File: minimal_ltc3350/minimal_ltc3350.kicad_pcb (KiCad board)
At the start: 4 copper layers, 25.4 x 25.4 mm, 0 parts

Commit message: Update KiCad project files (PCB layout, project settings, and schematic)
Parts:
- added U1: LTC3350EUHF-PBF, analog_devices_footprints:QFN-38_UHF_LIT, F.Cu at (139.7, 88.9)
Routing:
- added copper zone on B.Cu, net GND
- added copper zone on F.Cu, net GND
- added copper zone on In1.Cu, net GND
- added copper zone on In2.Cu, net GND
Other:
- outline, holes or cut-outs redrawn

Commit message: Update KiCad project files and submodule reference
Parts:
- added C1: 100 nF, capacitor_footprints:C_0402_1005Metric, F.Cu at (139.6, 83.8)
- added C2: 1 µF, capacitor_footprints:C_0603_1608Metric, F.Cu at (142.3, 83.8)
- added Q1: 20.0 V, transistor_footprints:PowerPAK 1212-8, F.Cu at (143.0, 80.9)
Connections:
- U1 pad 31: unconnected-(U1-VOUTSP-Pad31) -> /VOUTSP
- U1 pad 32: unconnected-(U1-VOUTM5-Pad32) -> /VOUTM5
- U1 pad 33: unconnected-(U1-INFET-Pad33) -> /INFET
- U1 pad 34: unconnected-(U1-VIN-Pad34) -> /VIN
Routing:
- net /INFET: track 0.00 -> 4.16 mm
- net /VOUTM5: track 0.00 -> 1.78 mm
- net /VIN: track 0.00 -> 1.71 mm

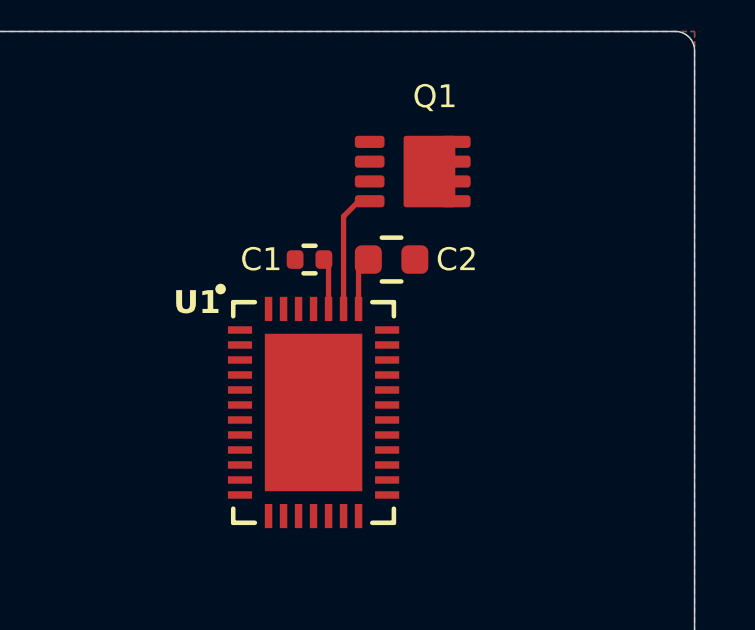
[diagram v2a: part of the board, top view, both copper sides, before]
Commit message: Add VOUT sensing resistor and update symbol libraries
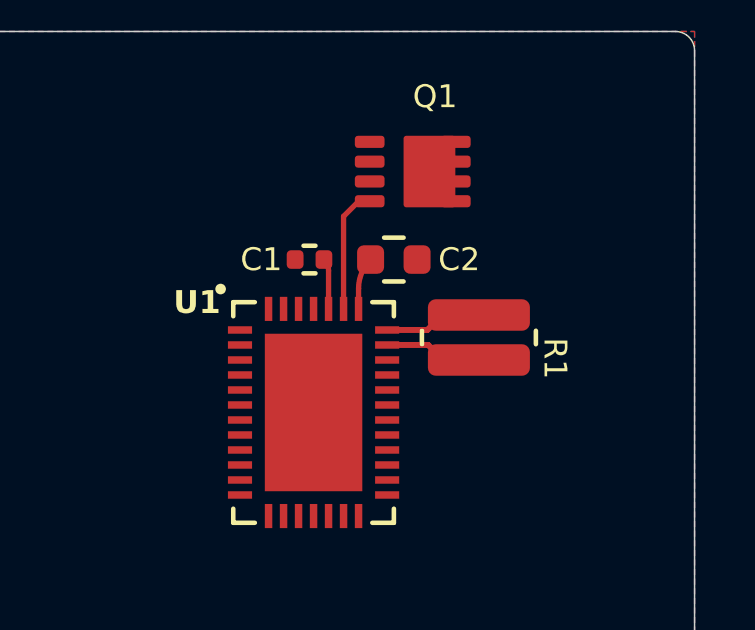
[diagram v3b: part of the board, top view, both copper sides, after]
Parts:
- added R1: 0.016 Ω, resistor_footprints:R_0612_1632Metric, F.Cu at (145.2, 86.4)
- moved C2 0.08 mm to (142.4, 83.8)
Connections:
- U1 pad 30: unconnected-(U1-VOUTSN-Pad30) -> /VOUT
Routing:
- net /VOUT: track 0.00 -> 3.27 mm
- net /VOUTSP: track 0.00 -> 3.27 mm

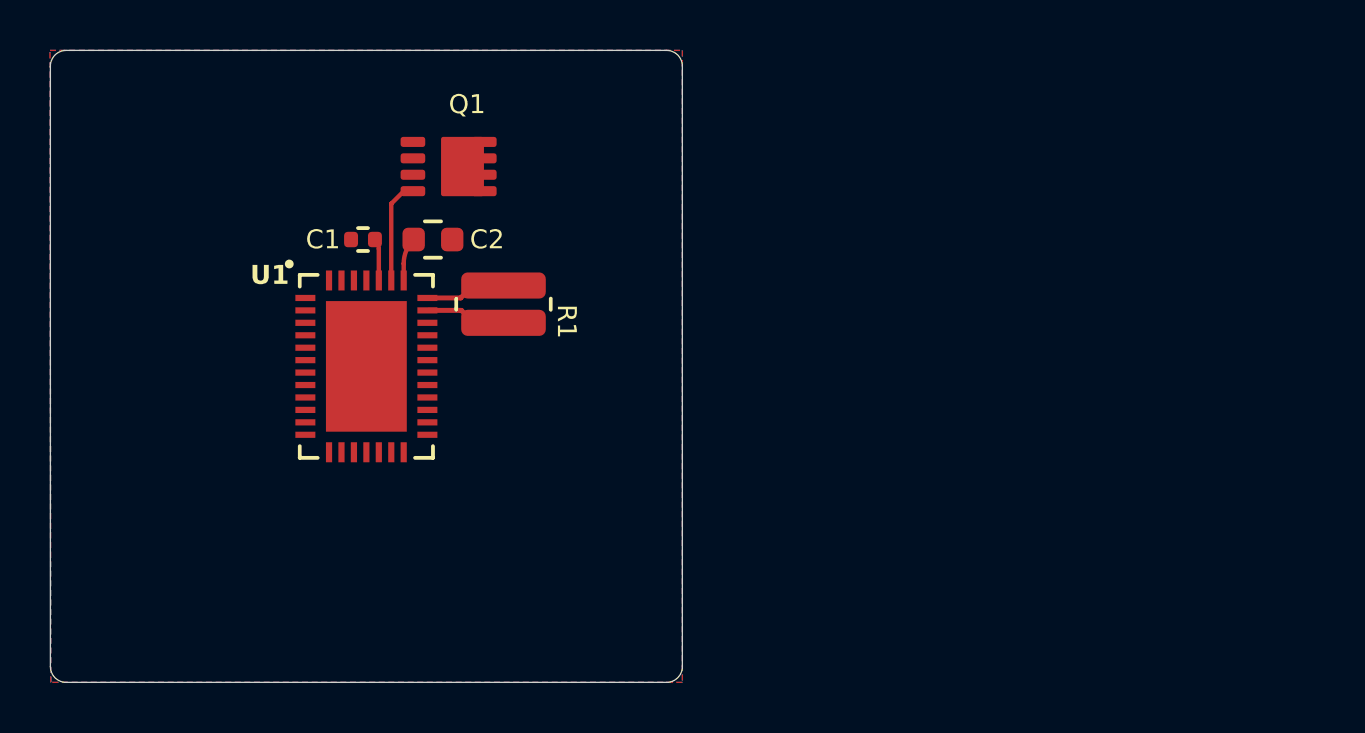
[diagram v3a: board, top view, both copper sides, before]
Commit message: Update schematic and PCB with VOUT sensing resistor and component changes
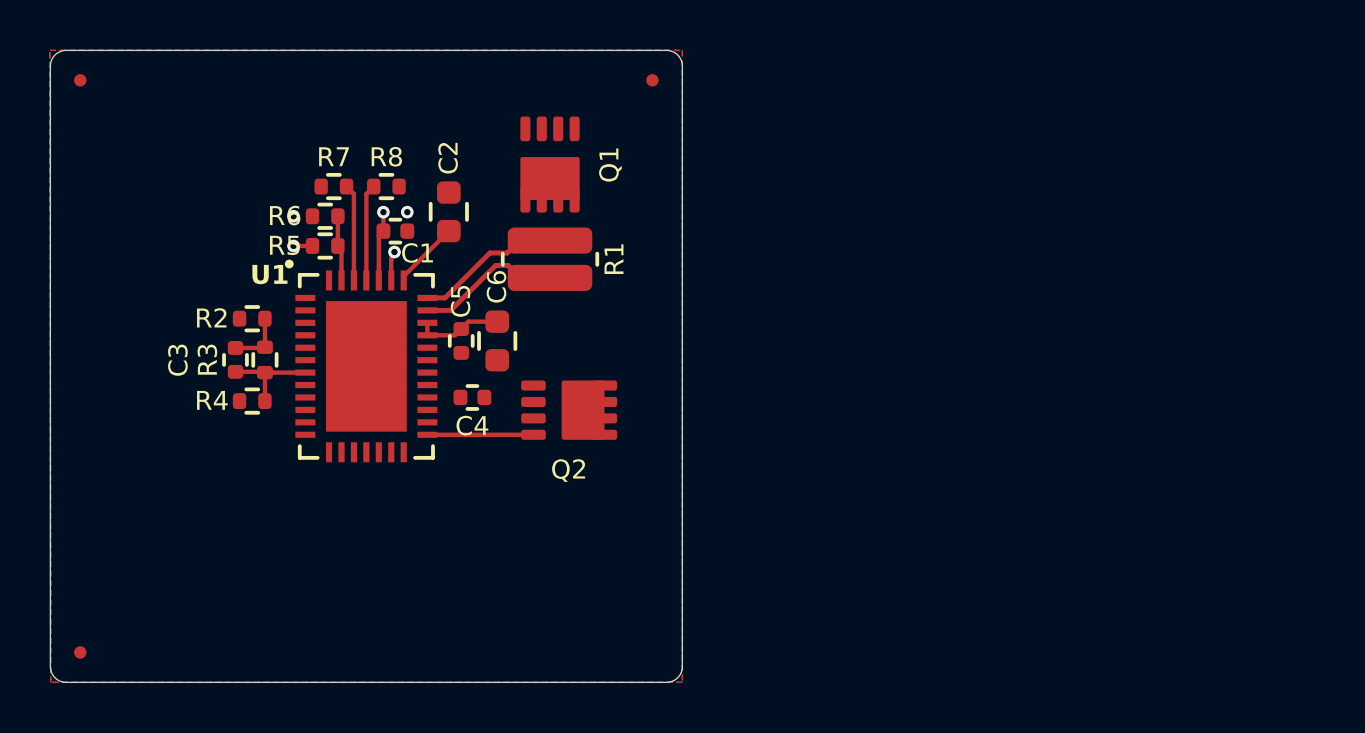
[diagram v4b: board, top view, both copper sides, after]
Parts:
- added C3: 120 pF, capacitor_footprints:C_0402_1005Metric, F.Cu at (134.4, 88.6)
- added C4: 1 µF, capacitor_footprints:C_0402_1005Metric, F.Cu at (144.0, 90.2)
- added C5: 100 nF, capacitor_footprints:C_0402_1005Metric, F.Cu at (143.5, 87.9)
- added C6: 4.7 µF, capacitor_footprints:C_0603_1608Metric, F.Cu at (145.0, 87.9)
- added FID1: Fiducial, no_components_footprints:Fiducial_0.5mm_Mask1mm, F.Cu at (128.2, 100.4)
- added FID2: Fiducial, no_components_footprints:Fiducial_0.5mm_Mask1mm, F.Cu at (128.2, 77.4)
- added FID3: Fiducial, no_components_footprints:Fiducial_0.5mm_Mask1mm, F.Cu at (151.2, 77.4)
- added Q2: 20.0 V, transistor_footprints:PowerPAK 1212-8, F.Cu at (147.9, 90.7)
- added R2: 20 Ω, resistor_footprints:R_0402_1005Metric, F.Cu at (135.1, 87.0)
- added R3: 649 kΩ, resistor_footprints:R_0402_1005Metric, F.Cu at (135.6, 88.6)
- added R4: 162 kΩ, resistor_footprints:R_0402_1005Metric, F.Cu at (135.1, 90.3)
- added R5: 787 kΩ, resistor_footprints:R_0402_1005Metric, F.Cu at (138.0, 84.1)
- added R6: 100 kΩ, resistor_footprints:R_0402_1005Metric, F.Cu at (138.0, 82.9)
- added R7: 100 kΩ, resistor_footprints:R_0402_1005Metric, F.Cu at (138.4, 81.7)
- added R8: 100 kΩ, resistor_footprints:R_0402_1005Metric, F.Cu at (140.5, 81.7)
- moved Q1 4.08 mm to (147.1, 80.8), turned to -90 degrees
- moved R1 2.60 mm to (147.1, 84.6)
- moved C1 1.34 mm to (140.9, 83.5), turned to 0 degrees
- moved C2 1.28 mm to (143.0, 82.7), turned to -90 degrees
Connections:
- U1 pad 20: unconnected-(U1-OUTFET-Pad20) -> /OUTFET
- U1 pad 23: unconnected-(U1-VCC2P5-Pad23) -> /VCC2P5
- U1 pad 28: unconnected-(U1-DRVCC-Pad28) -> /INTVCC
- U1 pad 29: unconnected-(U1-INTVCC-Pad29) -> /INTVCC
- U1 pad 35: unconnected-(U1-CAP_SLCT0-Pad35) -> /CAP_SLCT0
- U1 pad 36: unconnected-(U1-CAP_SLCT1-Pad36) -> /CAP_SLCT1
- U1 pad 37: unconnected-(U1-PFI-Pad37) -> /PFI
- U1 pad 7: unconnected-(U1-OUTFB-Pad7) -> /OUTFB
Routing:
- net /OUTFET: track 0.00 -> 4.26 mm
- net /OUTFB: track 0.00 -> 3.96 mm
- net /CAP_SLCT0: track 0.00 -> 3.90 mm
- net /CAP_SLCT1: track 0.00 -> 3.90 mm
- net /INTVCC: track 0.00 -> 3.53 mm
- net /INFET: track 4.16 -> 1.18 mm, vias 0 -> 1
- net /PFI: track 0.00 -> 2.64 mm
- net /VOUTSP: track 3.27 -> 5.88 mm
- net /VOUT: track 3.27 -> 5.88 mm
- net Net-(C3-Pad1): track 0.00 -> 2.34 mm
- net /VIN: track 1.68 -> 3.58 mm, vias 0 -> 2
- net /VOUTM5: track 1.75 -> 2.73 mm
- net GND: vias 0 -> 2

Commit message: Update KiCad project: Component changes and layout improvements
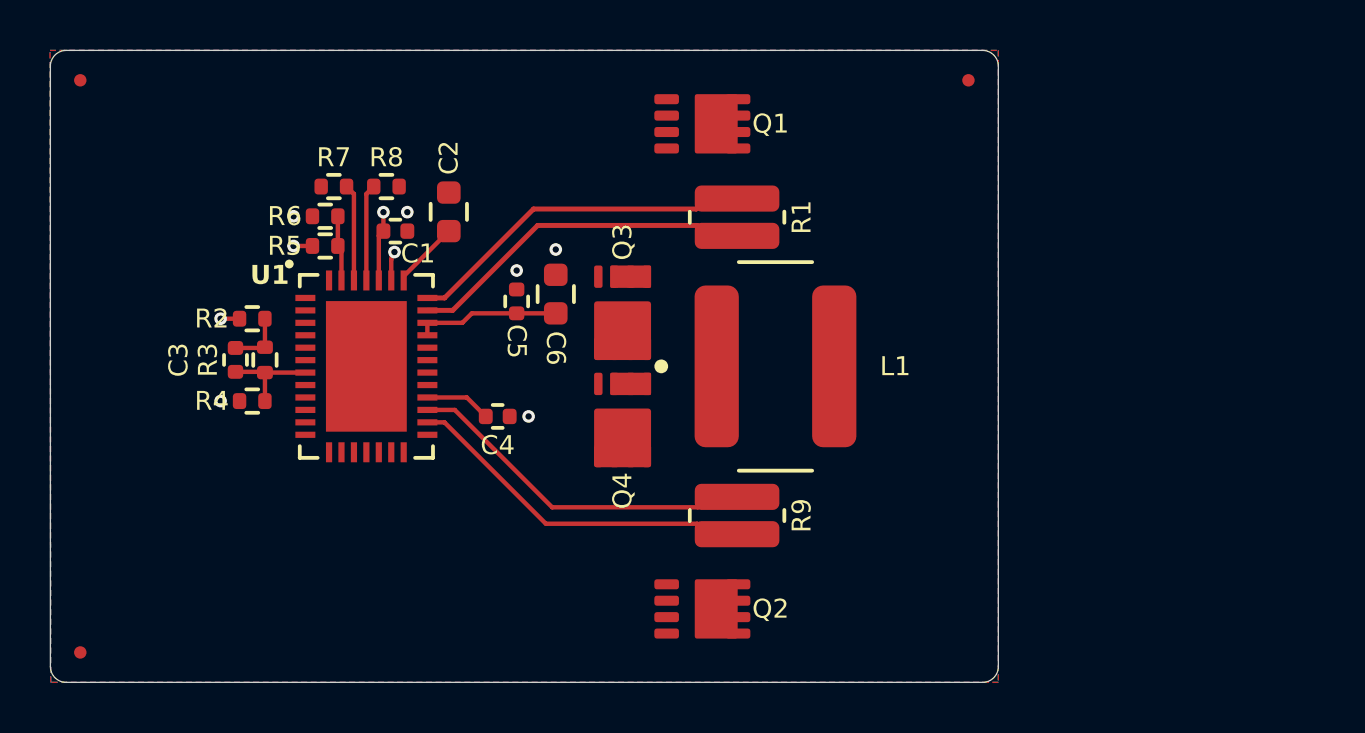
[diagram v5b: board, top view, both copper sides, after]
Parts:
- added L1: 3.3 µH, inductor_footprints:XAL7030, F.Cu at (156.1, 88.9)
- added Q3: 20 V, transistor_footprints:TSDSON-8FL, F.Cu at (150.0, 86.7)
- added Q4: 20 V, transistor_footprints:TSDSON-8FL, F.Cu at (150.0, 91.1)
- added R9: 0.006 Ω, resistor_footprints:R_0612_1632Metric, F.Cu at (154.6, 94.9)
- moved FID3 12.7 mm to (163.9, 77.4)
- moved Q2 9.62 mm to (153.2, 98.6)
- moved R1 7.71 mm to (154.6, 82.9)
- moved Q1 6.34 mm to (153.2, 79.2), turned to 0 degrees
- moved C6 3.02 mm to (147.3, 86.0), turned to 90 degrees
- moved C5 2.74 mm to (145.7, 86.3), turned to 90 degrees
- moved C4 1.27 mm to (145.0, 90.9)
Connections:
- Q2 pad 5: unconnected-(Q2-D-Pad5) -> Net-(Q2-D)
- U1 pad 21: unconnected-(U1-VCAP-Pad21) -> Net-(Q2-D)
- U1 pad 22: unconnected-(U1-ICAP-Pad22) -> Net-(U1-ICAP)
- U1 pad 24: unconnected-(U1-SW-Pad24) -> /SW
- U1 pad 25: unconnected-(U1-TGATE-Pad25) -> /TGATE
- U1 pad 27: unconnected-(U1-BGATE-Pad27) -> /BGATE
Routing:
- net Net-(Q2-D): track 0.00 -> 14.3 mm
- net Net-(U1-ICAP): track 0.00 -> 14.2 mm
- net /VOUT: track 5.88 -> 14.8 mm, vias 0 -> 1
- net /VOUTSP: track 5.88 -> 14.1 mm
- net /OUTFET: track 4.26 -> 0.00 mm
- net /VCC2P5: track 0.00 -> 2.66 mm
- net /INTVCC: track 3.53 -> 5.82 mm
- net GND: vias 2 -> 6
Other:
- board size 25.4 x 25.4 mm -> 38.1 x 25.4 mm

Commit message: Update KiCad project: Component changes, net updates, and symbol library additions
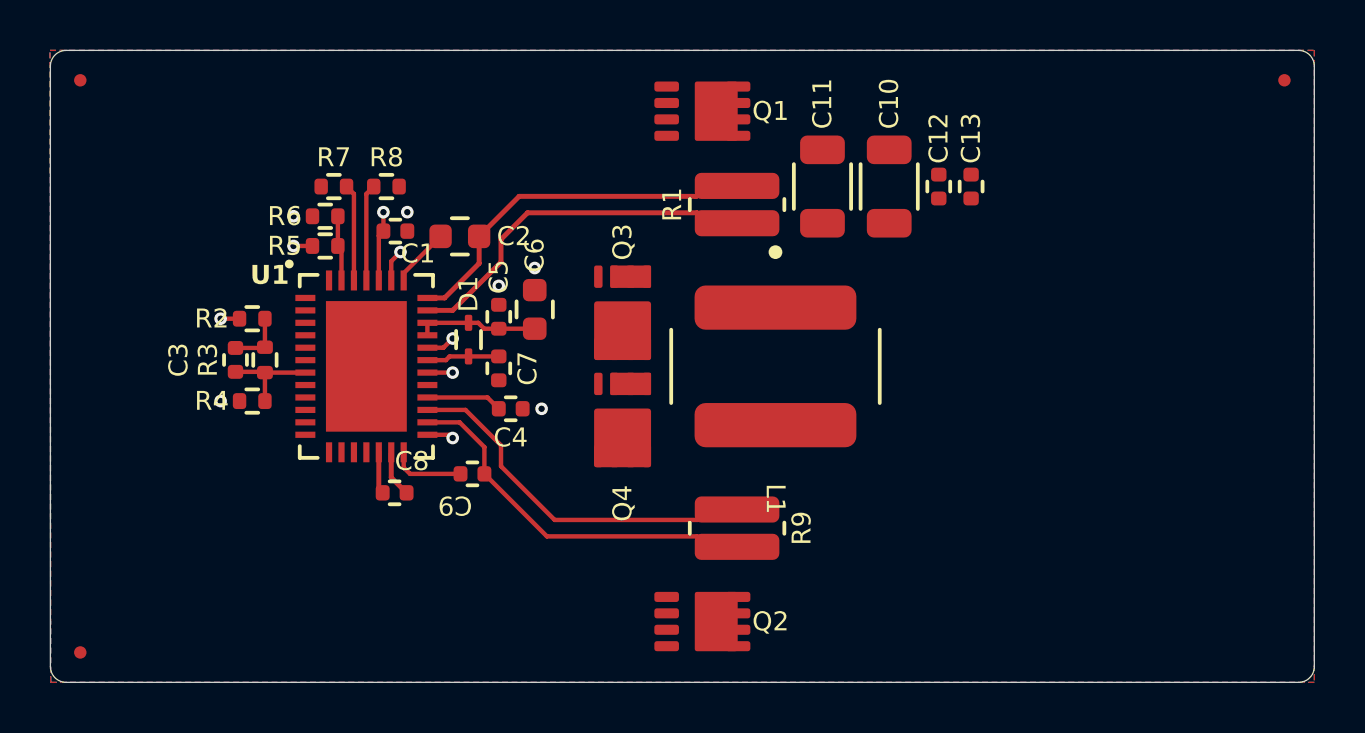
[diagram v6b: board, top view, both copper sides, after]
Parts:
- added C10: 47 µF, capacitor_footprints:C_1206_3216Metric, F.Cu at (160.7, 81.7)
- added C11: 47 µF, capacitor_footprints:C_1206_3216Metric, F.Cu at (158.0, 81.7)
- added C12: 2.2 µF, capacitor_footprints:C_0402_1005Metric, F.Cu at (162.7, 81.7)
- added C13: 2.2 µF, capacitor_footprints:C_0402_1005Metric, F.Cu at (164.0, 81.7)
- added C7: 100 nF, capacitor_footprints:C_0402_1005Metric, F.Cu at (145.0, 89.0)
- added C8: 100 nF, capacitor_footprints:C_0402_1005Metric, F.Cu at (140.8, 94.0)
- added C9: 100 nF, capacitor_footprints:C_0402_1005Metric, F.Cu at (144.0, 93.2)
- added D1: 80.0 V, diode_footprints:SOD_523, F.Cu at (143.8, 87.8)
- moved FID3 12.7 mm to (176.6, 77.4)
- moved C2 1.08 mm to (143.5, 83.7), turned to 180 degrees
- moved C6 1.05 mm to (146.5, 86.6)
- moved C5 0.95 mm to (145.0, 86.9)
- moved C4 0.61 mm to (145.5, 90.6)
- moved R1 0.51 mm to (154.6, 82.4)
- moved R9 0.51 mm to (154.6, 95.4)
- moved Q1 0.51 mm to (153.2, 78.6)
- moved Q2 0.51 mm to (153.2, 99.2)
- turned L1 to -90 degrees
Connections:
- net Net-(Q2-D) renamed /VCAP
- net Net-(U1-ICAP) renamed /ICAP
- U1 pad 17: unconnected-(U1-CFP-Pad17) -> /CFP
- U1 pad 18: unconnected-(U1-CFN-Pad18) -> /CFN
- U1 pad 19: unconnected-(U1-VCAPP5-Pad19) -> /VCAPP5
- U1 pad 26: unconnected-(U1-BST-Pad26) -> /BST
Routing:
- net /VCAPP5: track 0.00 -> 3.00 mm
- net /BST: track 0.00 -> 2.93 mm
- net /CFN: track 0.00 -> 1.89 mm
- net /CFP: track 0.00 -> 1.69 mm
- net /BGATE: track 0.00 -> 1.33 mm, vias 0 -> 1
- net /OUTFET: track 0.00 -> 1.07 mm, vias 0 -> 1
- net /TGATE: track 0.00 -> 1.02 mm, vias 0 -> 1
- net /INTVCC: track 5.82 -> 4.91 mm
- net /VOUTSP: track 14.1 -> 14.9 mm
- net /VCAP: track 14.3 -> 15.1 mm
- net /VOUT: track 14.8 -> 15.5 mm
- net /ICAP: track 14.2 -> 14.9 mm
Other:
- board size 38.1 x 25.4 mm -> 50.8 x 25.4 mm

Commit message: Update KiCad project files: PCB layout, schematic, project settings, and symbols generator
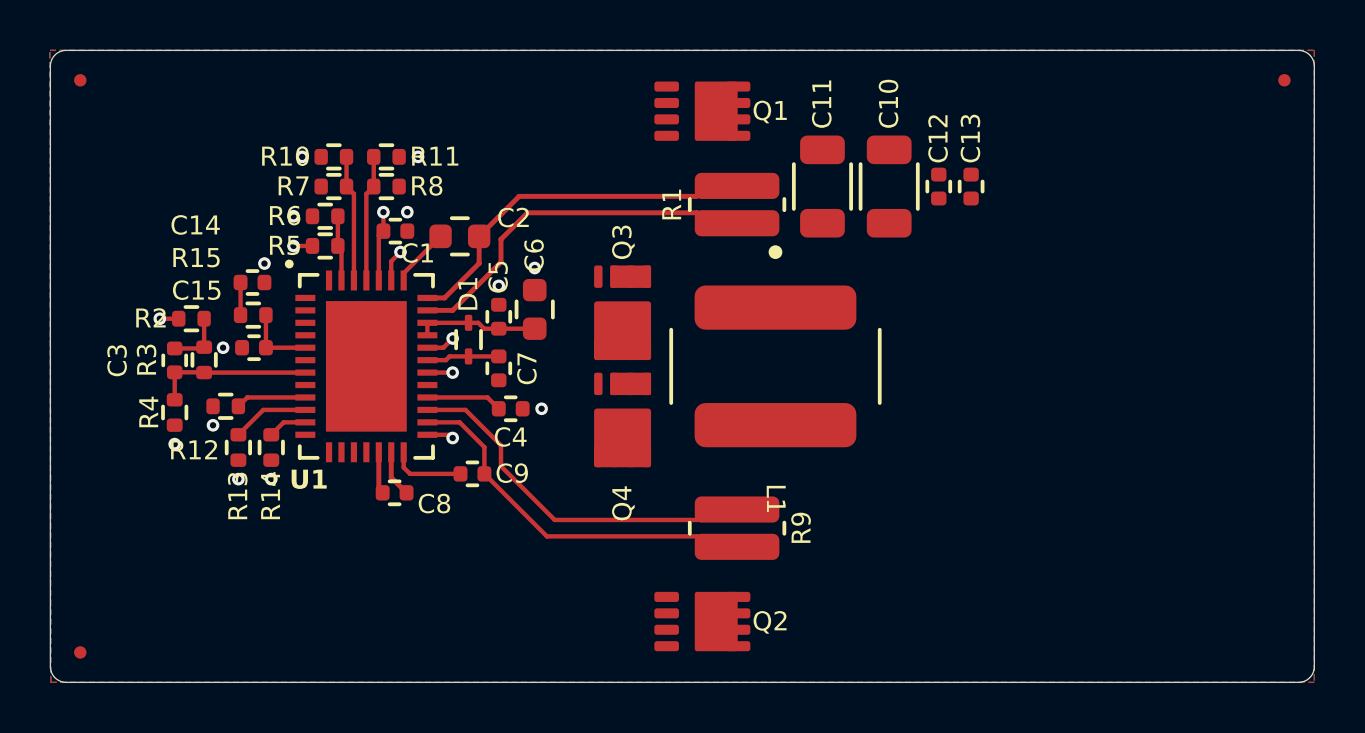
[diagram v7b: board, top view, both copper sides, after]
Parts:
- added C14: 10 nF, capacitor_footprints:C_0402_1005Metric, F.Cu at (135.1, 85.5)
- added C15: 10 nF, capacitor_footprints:C_0402_1005Metric, F.Cu at (135.2, 88.1)
- added R10: 0 Ω, resistor_footprints:R_0402_1005Metric, F.Cu at (138.4, 80.5)
- added R11: 0 Ω, resistor_footprints:R_0402_1005Metric, F.Cu at (140.5, 80.5)
- added R12: 71.5 kΩ, resistor_footprints:R_0402_1005Metric, F.Cu at (134.0, 90.5)
- added R13: 1 MΩ, resistor_footprints:R_0402_1005Metric, F.Cu at (134.6, 92.2)
- added R14: 121 Ω, resistor_footprints:R_0402_1005Metric, F.Cu at (135.9, 92.2)
- added R15: 0 Ω, resistor_footprints:R_0402_1005Metric, F.Cu at (135.2, 86.8)
- moved R4 3.15 mm to (132.0, 90.8), turned to -90 degrees
- moved C3 2.44 mm to (132.0, 88.7)
- moved R3 2.44 mm to (133.2, 88.6)
- moved R2 2.44 mm to (132.7, 87.0)
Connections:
- U1 pad 10: unconnected-(U1-GPI-Pad10) -> /GPI
- U1 pad 11: unconnected-(U1-ITST-Pad11) -> /ITST
- U1 pad 5: unconnected-(U1-VC-Pad5) -> /VC
- U1 pad 8: unconnected-(U1-SGND-Pad8) -> GND
- U1 pad 9: unconnected-(U1-RT-Pad9) -> /RT
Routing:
- net /GPI: track 0.00 -> 3.11 mm
- net /VC: track 0.00 -> 2.89 mm
- net /RT: track 0.00 -> 2.84 mm
- net /OUTFB: track 3.96 -> 6.16 mm
- net /ITST: track 0.00 -> 1.58 mm
- net Net-(C14-Pad1): track 0.00 -> 1.31 mm
- net /CAP_SLCT0: track 3.90 -> 5.09 mm
- net /CAP_SLCT1: track 3.90 -> 5.09 mm
- net GND: vias 6 -> 13

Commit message: Update KiCAD PCB and schematic files
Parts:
- added R16: 20 Ω, resistor_footprints:R_0402_1005Metric, F.Cu at (131.8, 85.6)
- added R17: 866 kΩ, resistor_footprints:R_0402_1005Metric, F.Cu at (131.8, 86.9)
- added R18: 118 kΩ, resistor_footprints:R_0402_1005Metric, F.Cu at (131.8, 88.2)
- moved R2 5.73 mm to (131.2, 92.5), turned to 90 degrees
- moved C3 2.09 mm to (131.8, 90.7), turned to 0 degrees
- moved R4 1.83 mm to (132.5, 92.5)
- moved R3 1.65 mm to (131.8, 89.6), turned to 0 degrees
- moved C14 0.96 mm to (134.2, 85.1)
- moved C15 0.96 mm to (134.3, 87.8)
- moved R15 0.96 mm to (134.3, 86.5)
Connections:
- U1 pad 6: unconnected-(U1-CAPFB-Pad6) -> /CAPFB
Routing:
- net /CAPFB: track 0.00 -> 6.42 mm
- net /OUTFB: track 6.16 -> 7.67 mm
- net Net-(R16-Pad2): track 0.00 -> 1.32 mm
- net /VC: track 2.89 -> 3.94 mm
- net /VCAP: track 15.1 -> 15.9 mm, vias 0 -> 1
- net GND: vias 13 -> 14
